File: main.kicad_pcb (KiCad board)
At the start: 2 copper layers, 65 x 56 mm, 73 parts, among them J2 mini iso blue, J3 LCD power, J7 Programming Socket, P1 Conn_02x20_Odd_Even, Q1 NPN, Q2 NPN, SW1 EN, SW2 EN, U1 TJA1051TK-3, U10 NTS0104GU12_115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

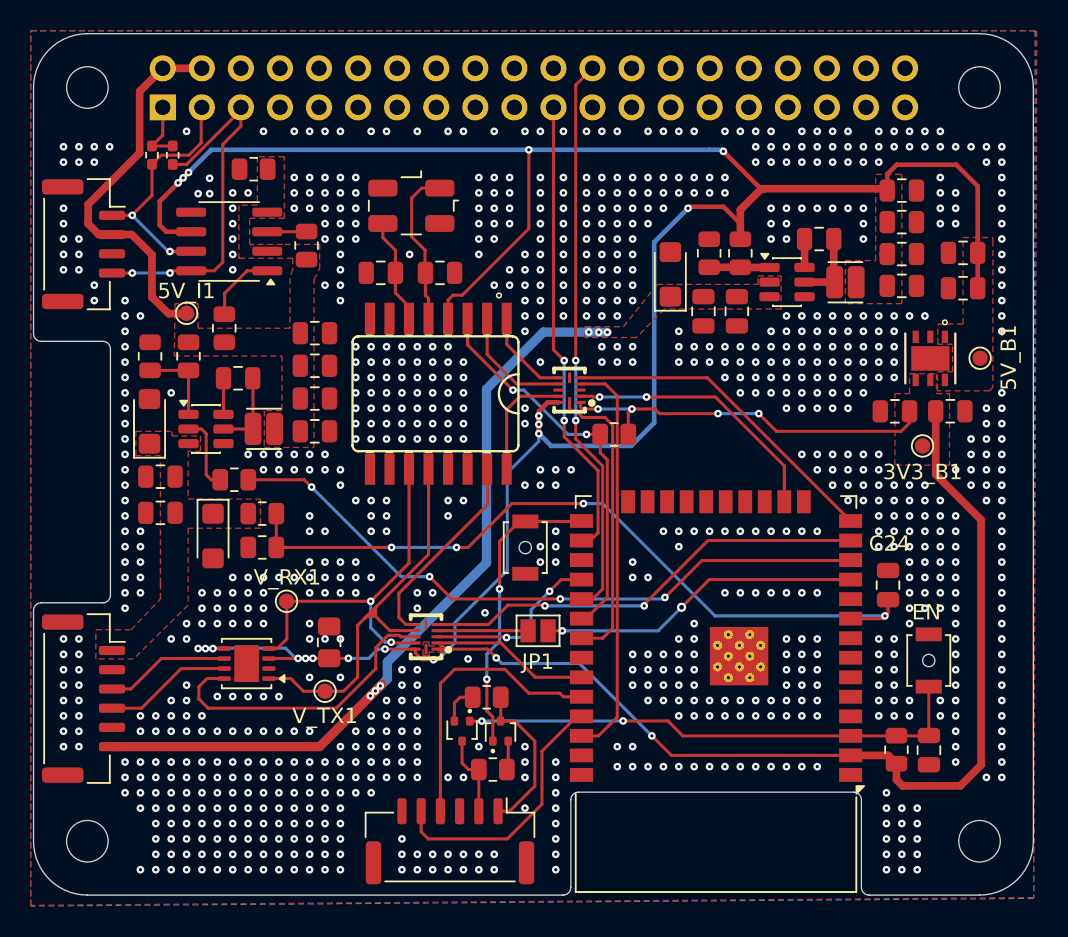
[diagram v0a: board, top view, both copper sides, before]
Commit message: Change inductor type.
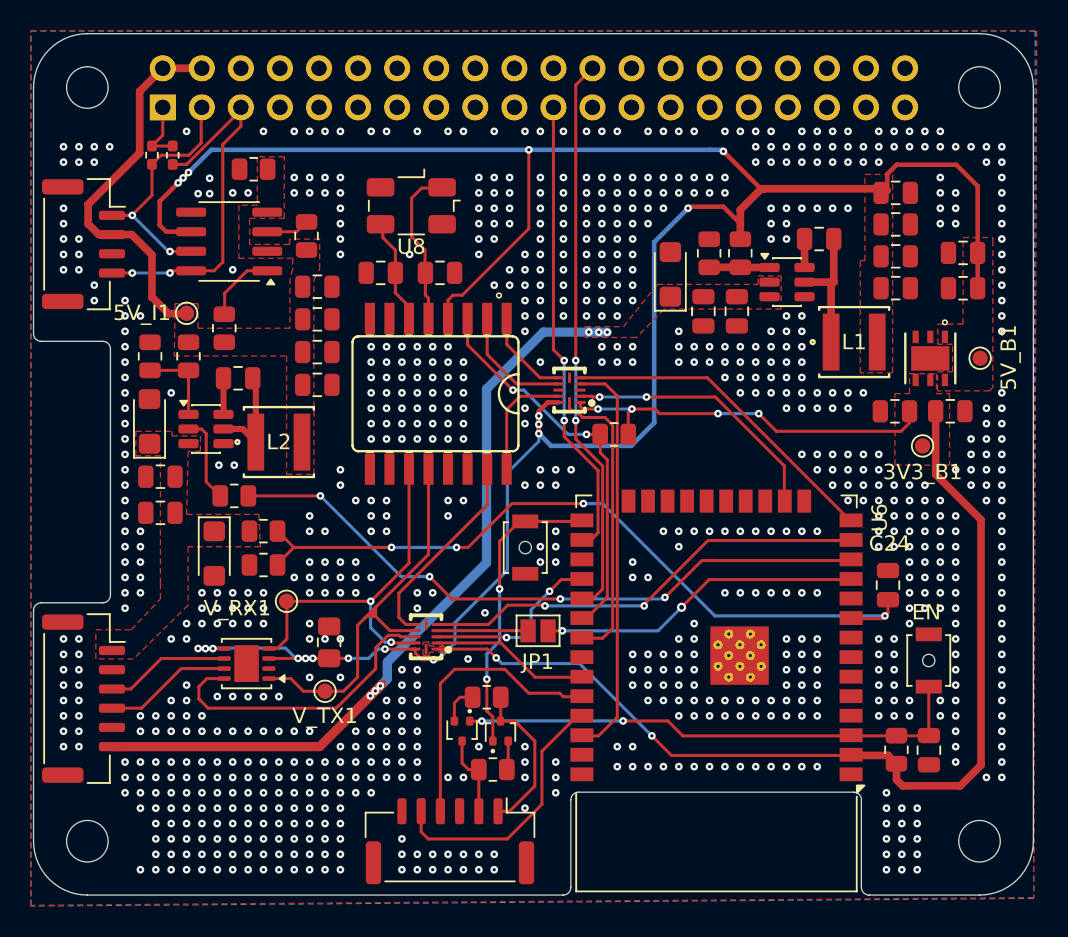
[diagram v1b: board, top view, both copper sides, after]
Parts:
- L1, L2: value VLS201612HBX-6R8M-1 -> 4.7uH; footprint Inductor_SMD:L_Cenker_CKCS201610 -> footprints:IND_TYA40204_LRD
- U6: footprint intoftainment:esp32_altered -> RF_Module:ESP32-WROOM-32D
- U8: footprint Crystal:Crystal_SMD_EuroQuartz_MJ-4Pin_5.0x3.2mm -> Crystal:Crystal_SMD_Abracon_ABM3B-4Pin_5.0x3.2mm
- moved U6 13.6 mm to (148.1, 121.1)
- moved L1 3.93 mm to (157.0, 101.2)
- moved C19 3.02 mm to (122.1, 104.0)
- moved C20 3.02 mm to (122.1, 101.9)
- moved C21 3.02 mm to (122.1, 99.8)
- moved C22 3.02 mm to (122.1, 97.6)
- moved L2 1.30 mm to (119.6, 107.7)
- moved U13 1.14 mm to (115.4, 115.0)
- moved R2 1.14 mm to (118.6, 113.5)
- moved R3 1.14 mm to (118.6, 115.7)
- moved R122 1.05 mm to (116.7, 111.2)
- moved R7 0.62 mm to (121.4, 94.3)
- moved C14 0.43 mm to (159.7, 93.6)
- moved C15 0.43 mm to (159.7, 95.7)
- moved C23 0.43 mm to (159.7, 97.7)
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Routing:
- net Net-(U4-SW): track 4.72 -> 8.70 mm
- net Net-(U5-SW): track 5.22 -> 6.70 mm
- net Net-(U5-EN): track 5.00 -> 5.70 mm
- net +5V Car Battery: track 158.1 -> 157.6 mm
- net GND: vias 946 -> 868

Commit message: Update bom values with actual chip names
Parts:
- C3: value 0.1uF -> 100nF; footprint Capacitor_SMD:C_0805_2012Metric_Pad1.18x1.45mm_HandSolder -> Capacitor_SMD:C_0805_2012Metric
- Q1, Q2: value NPN -> MMBT2222ATT3G
- R9: value 4k7 -> 4.7K
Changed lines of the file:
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@@
 			)
 		)
-		(property "Description" "Unpolarized capacitor"
+		(property "Description" ""
 			(at 0 0 0)
 			(layer "F.Fab")
@@
 			)
 		)
-		(property "Value" "4k7"
+		(property "Value" "4.7K"
 			(at 0 1.65 0)
 			(layer "F.Fab")
@@
 			)
 		)
-		(property "Description" "Unpolarized capacitor"
+		(property "Description" ""
 			(at 0 0 0)
 			(layer "F.Fab")
@@
 			)
 		)
-		(property "Description" "Unpolarized capacitor"
+		(property "Description" ""
 			(at 0 0 0)
 			(layer "F.Fab")
@@
 			)
 		)
-		(property "Description" "Unpolarized capacitor"
+		(property "Description" ""
 			(at 0 0 0)
 			(layer "F.Fab")
@@
 			)
 		)
-		(property "Description" "Unpolarized capacitor"
+		(property "Description" ""
 			(at 0 0 0)
 			(layer "F.Fab")
@@
 			)
 		)
-		(property "Description" "Unpolarized capacitor"
+		(property "Description" ""
 			(at 0 0 180)
 			(layer "F.Fab")
@@
 			)
 		)
-		(property "Description" "Unpolarized capacitor"
+		(property "Description" ""
 			(at 0 0 90)
 			(layer "F.Fab")
@@
 			)
 		)
-		(property "Description" "Unpolarized capacitor"
+		(property "Description" ""
 			(at 0 0 90)
 			(layer "F.Fab")
@@
 			)
 		)
-		(property "Description" "Unpolarized capacitor"
+		(property "Description" ""
 			(at 0 0 0)
 			(layer "F.Fab")
@@
 			)
 		)
-		(property "Description" "Generic connector, single row, 01x06, script generated"
+		(property "Description" ""
 			(at 0 0 90)
 			(layer "F.Fab")
@@
 			)
 		)
-		(property "Description" "Unpolarized capacitor"
+		(property "Description" ""
 			(at 0 0 90)
 			(layer "F.Fab")
@@
 			)
 		)
-		(property "Description" "Unpolarized capacitor"
+		(property "Description" ""
 			(at 0 0 0)
 			(layer "F.Fab")
@@
 			)
 		)
-		(property "Datasheet" ""
+		(property "Datasheet" "https://eu.mouser.com/datasheet/3/184/1/abm3b.pdf"
 			(at 0 0 180)
 			(layer "F.Fab")
@@
 			)
 		)
-		(property "Description" ""
+		(property "Description" "8 MHz crystal oscillator"
 			(at 0 0 180)
 			(layer "F.Fab")
@@
 			)
 		)
-		(property "Description" "Unpolarized capacitor"
+		(property "Description" ""
 			(at 0 0 0)
 			(layer "F.Fab")
@@
 			)
 		)
-		(property "Value" "NPN"
+		(property "Value" "MMBT2222ATT3G"
 			(at 0 2.25 90)
 			(layer "F.Fab")
@@
 			)
 		)
-		(property "Description" "Unpolarized capacitor"
+		(property "Description" ""
 			(at 0 0 0)
 			(layer "F.Fab")
@@
 			)
 		)
-		(property "Description" "Unpolarized capacitor"
+		(property "Description" ""
 			(at 0 0 0)
 			(layer "F.Fab")
@@
 		)
 	)
-	(footprint "Capacitor_SMD:C_0805_2012Metric_Pad1.18x1.45mm_HandSolder"
+	(footprint "Capacitor_SMD:C_0805_2012Metric"
 		(layer "F.Cu")
 		(at 122.9 120.76 90)
-		(descr "Capacitor SMD 0805 (2012 Metric), square (rectangular) end terminal, IPC-7351 nominal with elongated pad for handsoldering. (Body size source: IPC-SM-782 page 76, https://www.pcb-3d.com/wordpress/wp-content/uploads/ipc-sm-782a_amendment_1_and_2.pdf, https://docs.google.com/spreadsheets/d/1BsfQQcO9C6DZCsRaXUlFlo91Tg2WpOkGARC1WS5S8t0/edit?usp=sharing), generated with kicad-footprint-generator")
-		(tags "capacitor handsolder")
+		(descr "Capacitor SMD 0805 (2012 Metric), square (rectangular) end terminal, IPC-7351 nominal, (Body size source: IPC-SM-782 page 76, https://www.pcb-3d.com/wordpress/wp-content/uploads/ipc-sm-782a_amendment_1_and_2.pdf, https://docs.google.com/spreadsheets/d/1BsfQQcO9C6DZCsRaXUlFlo91Tg2WpOkGARC1WS5S8t0/edit?usp=sharing), generated with kicad-footprint-generator")
+		(tags "capacitor")
 		(property "Reference" "C3"
 			(at 0 -1.68 90)
 			(layer "F.SilkS")
-			(hide yes)
 			(effects
 				(font
@@
 			)
 		)
-		(property "Value" "0.1uF"
+		(property "Value" "100nF"
 			(at 0 1.68 90)
 			(layer "F.Fab")
@@
 			)
 		)
-		(property "Description" "Unpolarized capacitor"
+		(property "Description" ""
 			(at 0 0 90)
 			(layer "F.Fab")
@@
 			(layer "F.SilkS")
 		)
-		(fp_line
-			(start 1.88 -0.98)
-			(end 1.88 0.98)
-			(stroke
-				(width 0.05)
-				(type solid)
-			)
-			(layer "F.CrtYd")
-		)
-		(fp_line
-			(start -1.88 -0.98)
-			(end 1.88 -0.98)
-			(stroke
-				(width 0.05)
-				(type solid)
-			)
-			(layer "F.CrtYd")
-		)
-		(fp_line
-			(start 1.88 0.98)
-			(end -1.88 0.98)
-			(stroke
-				(width 0.05)
-				(type solid)
-			)
-			(layer "F.CrtYd")
-		)
-		(fp_line
-			(start -1.88 0.98)
-			(end -1.88 -0.98)
+		(fp_rect
+			(start -1.7 -0.98)
+			(end 1.7 0.98)
 			(stroke
 				(width 0.05)
 				(type solid)
 			)
+			(fill no)
 			(layer "F.CrtYd")
 		)
-		(fp_line
-			(start 1 -0.625)
-			(end 1 0.625)
-			(stroke
-				(width 0.1)
-				(type solid)
-			)
-			(layer "F.Fab")
-		)
-		(fp_line
+		(fp_rect
 			(start -1 -0.625)
-			(end 1 -0.625)
-			(stroke
-				(width 0.1)
-				(type solid)
-			)
-			(layer "F.Fab")
-		)
-		(fp_line
-			(start 1 0.625)
-			(end -1 0.625)
-			(stroke
-				(width 0.1)
-				(type solid)
-			)
-			(layer "F.Fab")
-		)
-		(fp_line
-			(start -1 0.625)
-			(end -1 -0.625)
+			(end 1 0.625)
 			(stroke
 				(width 0.1)
 				(type solid)
 			)
+			(fill no)
 			(layer "F.Fab")
 		)
@@
 		)
 		(pad "1" smd roundrect
-			(at -1.0375 0 90)
-			(size 1.175 1.45)
+			(at -0.95 0 90)
+			(size 1 1.45)
 			(layers "F.Cu" "F.Mask" "F.Paste")
-			(roundrect_rratio 0.212766)
+			(roundrect_rratio 0.25)
 			(net 3 "+5V Car Battery")
 			(pintype "passive")
 		)
 		(pad "2" smd roundrect
-			(at 1.0375 0 90)
-			(size 1.175 1.45)
+			(at 0.95 0 90)
+			(size 1 1.45)
 			(layers "F.Cu" "F.Mask" "F.Paste")
-			(roundrect_rratio 0.212766)
+			(roundrect_rratio 0.25)
 			(net 1 "GND")
 			(pintype "passive")
 		)
 		(embedded_fonts no)
-		(model "${KICAD9_3DMODEL_DIR}/Capacitor_SMD.3dshapes/C_0805_2012Metric.wrl"
+		(model "${KICAD9_3DMODEL_DIR}/Capacitor_SMD.3dshapes/C_0805_2012Metric.step"
 			(offset
 				(xyz 0 0 0)
@@
 			)
 		)
-		(property "Description" "Unpolarized capacitor"
+		(property "Description" ""
 			(at 0 0 0)
 			(layer "F.Fab")
@@
 			)
 		)
-		(property "Description" "Generic connector, single row, 01x04, script generated"
+		(property "Description" ""
 			(at 0 0 90)
 			(layer "F.Fab")
@@
 			)
 		)
-		(property "Description" "Unpolarized capacitor"
+		(property "Description" ""
 			(at 0 0 0)
 			(layer "F.Fab")
@@
 			)
 		)
-		(property "Description" "Unpolarized capacitor"
+		(property "Description" ""
 			(at 0 0 90)
 			(layer "F.Fab")
@@
 			)
 		)
-		(property "Value" "NPN"
+		(property "Value" "MMBT2222ATT3G"
 			(at 0 2.25 90)
 			(layer "F.Fab")
@@
 			)
 		)
-		(property "Description" "Generic connector, single row, 01x06, script generated"
+		(property "Description" ""
 			(at 0 0 0)
 			(layer "F.Fab")
@@
 			)
 		)
-		(property "Description" "Unpolarized capacitor"
+		(property "Description" ""
 			(at 0 0 0)
 			(layer "F.Fab")
@@
 			)
 		)
-		(property "Description" "Unpolarized capacitor"
+		(property "Description" ""
 			(at 0 0 0)
 			(layer "F.Fab")
@@
 			)
 		)
-		(property "Description" "Unpolarized capacitor"
+		(property "Description" ""
 			(at 0 0 0)
 			(layer "F.Fab")
@@
 			)
 		)
-		(property "Description" "Unpolarized capacitor"
+		(property "Description" ""
 			(at 0 0 0)
 			(layer "F.Fab")
@@
 			)
 		)
-		(property "Description" "Unpolarized capacitor"
+		(property "Description" ""
 			(at 0 0 0)
 			(layer "F.Fab")
@@
 			)
 		)
-		(property "Description" "Unpolarized capacitor"
+		(property "Description" ""
 			(at 0 0 0)
 			(layer "F.Fab")
